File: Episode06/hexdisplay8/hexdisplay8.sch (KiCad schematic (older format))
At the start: 18 parts, among them J1 Conn_02x05_Counter_Clockwise, J2 Conn_02x05_Counter_Clockwise, J3 Conn_01x02, J4 Conn_01x08, J5 Conn_01x06, Q1 MMBT3906, Q2 MMBT3906

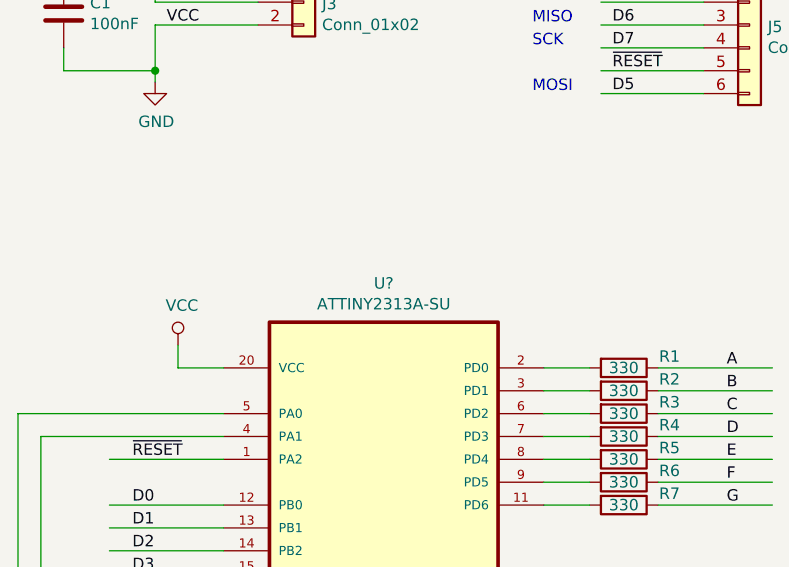
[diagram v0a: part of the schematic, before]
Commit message: assign packages
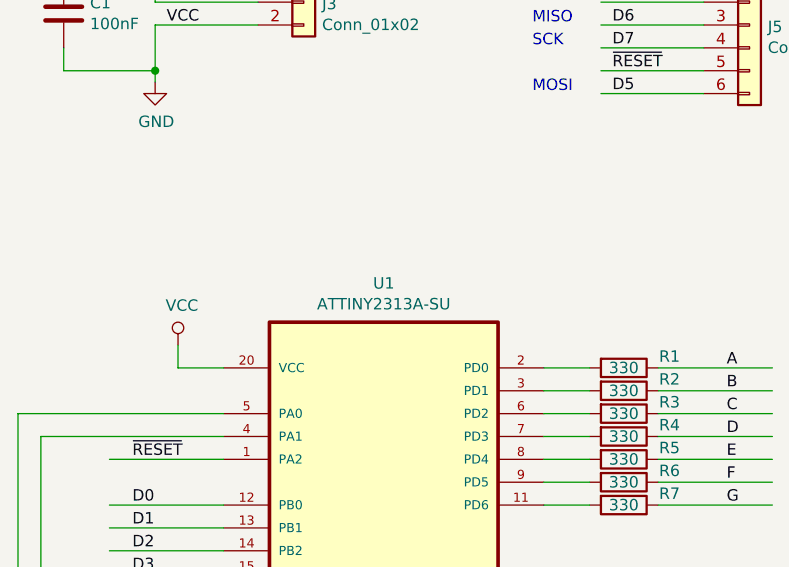
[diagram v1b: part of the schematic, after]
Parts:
- C1: footprint (none) -> Capacitor_SMD:C_1206_3216Metric_Pad1.33x1.80mm_HandSolder
- J1, J2: footprint (none) -> Package_DIP:DIP-10_W7.62mm
- J3: footprint (none) -> Connector_PinHeader_2.54mm:PinHeader_1x02_P2.54mm_Vertical
- J4: footprint (none) -> Connector_PinHeader_2.54mm:PinHeader_1x08_P2.54mm_Vertical
- J5: footprint (none) -> Connector_PinHeader_2.54mm:PinHeader_1x06_P2.54mm_Vertical
- Q1, Q2: footprint SOT95P240X120-3N -> Package_TO_SOT_SMD:SOT-23
- R1, R2, R3, R4, R5, R6, R7, R8, R9: footprint (none) -> Resistor_SMD:R_0805_2012Metric_Pad1.20x1.40mm_HandSolder
- U1: renamed from U?; footprint SOIC127P1032X265-20N -> Package_QFP:LQFP-44_10x10mm_P0.8mm
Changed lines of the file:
@@
 $EndDescr
 $Comp
-L ATTINY2313A-SU:ATTINY2313A-SU U?
+L ATTINY2313A-SU:ATTINY2313A-SU U1
 U 1 1 60451980
 P 2750 3800
-F 0 "U?" H 2750 4770 50  0000 C CNN
+F 0 "U1" H 2750 4770 50  0000 C CNN
 F 1 "ATTINY2313A-SU" H 2750 4679 50  0000 C CNN
-F 2 "SOIC127P1032X265-20N" H 2750 3800 50  0001 L BNN
+F 2 "Package_QFP:LQFP-44_10x10mm_P0.8mm" H 2750 3800 50  0001 L BNN
 F 3 "" H 2750 3800 50  0001 L BNN
 F 4 "Atmel" H 2750 3800 50  0001 L BNN "SUPPLIER"
@@
 F 0 "J2" H 8000 4267 50  0000 C CNN
 F 1 "Conn_02x05_Counter_Clockwise" H 8000 4176 50  0000 C CNN
-F 2 "" H 7950 3850 50  0001 C CNN
+F 2 "Package_DIP:DIP-10_W7.62mm" H 7950 3850 50  0001 C CNN
 F 3 "" H 7950 3850 50  0001 C CNN
 	1    7950 3850
@@
 F 0 "Q1" H 3353 5996 50  0000 L CNN
 F 1 "MMBT3906" H 3353 5905 50  0000 L CNN
-F 2 "SOT95P240X120-3N" H 3200 5950 50  0001 L BNN
+F 2 "Package_TO_SOT_SMD:SOT-23" H 3200 5950 50  0001 L BNN
 F 3 "" H 3200 5950 50  0001 L BNN
 F 4 "Fairchild Semiconductor" H 3200 5950 50  0001 L BNN "MANUFACTURER"
@@
 F 0 "Q2" H 3503 6946 50  0000 L CNN
 F 1 "MMBT3906" H 3503 6855 50  0000 L CNN
-F 2 "SOT95P240X120-3N" H 3350 6900 50  0001 L BNN
+F 2 "Package_TO_SOT_SMD:SOT-23" H 3350 6900 50  0001 L BNN
 F 3 "" H 3350 6900 50  0001 L BNN
 F 4 "Fairchild Semiconductor" H 3350 6900 50  0001 L BNN "MANUFACTURER"
@@
 F 0 "J1" H 8000 3217 50  0000 C CNN
 F 1 "Conn_02x05_Counter_Clockwise" H 8000 3126 50  0000 C CNN
-F 2 "" H 7950 2800 50  0001 C CNN
+F 2 "Package_DIP:DIP-10_W7.62mm" H 7950 2800 50  0001 C CNN
 F 3 "" H 7950 2800 50  0001 C CNN
 	1    7950 2800
@@
 F 0 "J5" H 4430 1692 50  0000 L CNN
 F 1 "Conn_01x06" H 4430 1601 50  0000 L CNN
-F 2 "" H 4350 1700 50  0001 C CNN
+F 2 "Connector_PinHeader_2.54mm:PinHeader_1x06_P2.54mm_Vertical" H 4350 1700 50  0001 C CNN
 F 3 "" H 4350 1700 50  0001 C CNN
 	1    4350 1700
@@
 	1850 3200 1850 3100
 $Comp
-L power:VCC #PWR?
+L power:VCC #PWR0101
 U 1 1 60461FFF
 P 1850 3100
-F 0 "#PWR?" H 1850 2950 50  0001 C CNN
+F 0 "#PWR0101" H 1850 2950 50  0001 C CNN
 F 1 "VCC" H 1867 3273 50  0000 C CNN
 F 2 "" H 1850 3100 50  0001 C CNN
@@
 	1850 4700 1850 4850
 $Comp
-L power:GND #PWR?
+L power:GND #PWR0102
 U 1 1 60462A72
 P 1850 4850
-F 0 "#PWR?" H 1850 4600 50  0001 C CNN
+F 0 "#PWR0102" H 1850 4600 50  0001 C CNN
 F 1 "GND" H 1855 4677 50  0000 C CNN
 F 2 "" H 1850 4850 50  0001 C CNN
@@
 F 0 "R1" V 3750 3400 50  0000 C CNN
 F 1 "330" V 3800 3200 50  0000 C CNN
-F 2 "" V 3730 3200 50  0001 C CNN
+F 2 "Resistor_SMD:R_0805_2012Metric_Pad1.20x1.40mm_HandSolder" V 3730 3200 50  0001 C CNN
 F 3 "" H 3800 3200 50  0001 C CNN
 	1    3800 3200
@@
 F 0 "R2" V 3750 3500 50  0000 C CNN
 F 1 "330" V 3800 3300 50  0000 C CNN
-F 2 "" V 3730 3300 50  0001 C CNN
+F 2 "Resistor_SMD:R_0805_2012Metric_Pad1.20x1.40mm_HandSolder" V 3730 3300 50  0001 C CNN
 F 3 "" H 3800 3300 50  0001 C CNN
 	1    3800 3300
@@
 F 0 "R3" V 3750 3600 50  0000 C CNN
 F 1 "330" V 3800 3400 50  0000 C CNN
-F 2 "" V 3730 3400 50  0001 C CNN
+F 2 "Resistor_SMD:R_0805_2012Metric_Pad1.20x1.40mm_HandSolder" V 3730 3400 50  0001 C CNN
 F 3 "" H 3800 3400 50  0001 C CNN
 	1    3800 3400
@@
 F 0 "R4" V 3750 3700 50  0000 C CNN
 F 1 "330" V 3800 3500 50  0000 C CNN
-F 2 "" V 3730 3500 50  0001 C CNN
+F 2 "Resistor_SMD:R_0805_2012Metric_Pad1.20x1.40mm_HandSolder" V 3730 3500 50  0001 C CNN
 F 3 "" H 3800 3500 50  0001 C CNN
 	1    3800 3500
@@
 F 0 "R5" V 3750 3800 50  0000 C CNN
 F 1 "330" V 3800 3600 50  0000 C CNN
-F 2 "" V 3730 3600 50  0001 C CNN
+F 2 "Resistor_SMD:R_0805_2012Metric_Pad1.20x1.40mm_HandSolder" V 3730 3600 50  0001 C CNN
 F 3 "" H 3800 3600 50  0001 C CNN
 	1    3800 3600
@@
 F 0 "R6" V 3750 3900 50  0000 C CNN
 F 1 "330" V 3800 3700 50  0000 C CNN
-F 2 "" V 3730 3700 50  0001 C CNN
+F 2 "Resistor_SMD:R_0805_2012Metric_Pad1.20x1.40mm_HandSolder" V 3730 3700 50  0001 C CNN
 F 3 "" H 3800 3700 50  0001 C CNN
 	1    3800 3700
@@
 F 0 "R7" V 3750 4000 50  0000 C CNN
 F 1 "330" V 3800 3800 50  0000 C CNN
-F 2 "" V 3730 3800 50  0001 C CNN
+F 2 "Resistor_SMD:R_0805_2012Metric_Pad1.20x1.40mm_HandSolder" V 3730 3800 50  0001 C CNN
 F 3 "" H 3800 3800 50  0001 C CNN
 	1    3800 3800
@@
 F 0 "R8" V 2550 5950 50  0000 C CNN
 F 1 "4k7" V 2650 5950 50  0000 C CNN
-F 2 "" V 2580 5950 50  0001 C CNN
+F 2 "Resistor_SMD:R_0805_2012Metric_Pad1.20x1.40mm_HandSolder" V 2580 5950 50  0001 C CNN
 F 3 "" H 2650 5950 50  0001 C CNN
 	1    2650 5950
@@
 F 0 "R9" V 2700 6900 50  0000 C CNN
 F 1 "4k7" V 2800 6900 50  0000 C CNN
-F 2 "" V 2730 6900 50  0001 C CNN
+F 2 "Resistor_SMD:R_0805_2012Metric_Pad1.20x1.40mm_HandSolder" V 2730 6900 50  0001 C CNN
 F 3 "" H 2800 6900 50  0001 C CNN
 	1    2800 6900
@@
 	4300 5450 4300 5250
 $Comp
-L power:VCC #PWR?
+L power:VCC #PWR0103
 U 1 1 6048B22B
 P 4300 5250
-F 0 "#PWR?" H 4300 5100 50  0001 C CNN
+F 0 "#PWR0103" H 4300 5100 50  0001 C CNN
 F 1 "VCC" H 4317 5423 50  0000 C CNN
 F 2 "" H 4300 5250 50  0001 C CNN
@@
 F 0 "J3" H 2480 1592 50  0000 L CNN
 F 1 "Conn_01x02" H 2480 1501 50  0000 L CNN
-F 2 "" H 2400 1600 50  0001 C CNN
+F 2 "Connector_PinHeader_2.54mm:PinHeader_1x02_P2.54mm_Vertical" H 2400 1600 50  0001 C CNN
 F 3 "" H 2400 1600 50  0001 C CNN
 	1    2400 1600
@@
 	1750 1950 1750 1900
 $Comp
-L power:VCC #PWR?
+L power:VCC #PWR0104
 U 1 1 604BADE0
 P 1750 1350
-F 0 "#PWR?" H 1750 1200 50  0001 C CNN
+F 0 "#PWR0104" H 1750 1200 50  0001 C CNN
 F 1 "VCC" H 1767 1523 50  0000 C CNN
 F 2 "" H 1750 1350 50  0001 C CNN
@@
 $EndComp
 $Comp
-L power:GND #PWR?
+L power:GND #PWR0105
 U 1 1 604BB1BF
 P 1750 1950
-F 0 "#PWR?" H 1750 1700 50  0001 C CNN
+F 0 "#PWR0105" H 1750 1700 50  0001 C CNN
 F 1 "GND" H 1755 1777 50  0000 C CNN
 F 2 "" H 1750 1950 50  0001 C CNN
@@
 F 0 "C1" H 1465 1696 50  0000 L CNN
 F 1 "100nF" H 1465 1605 50  0000 L CNN
-F 2 "" H 1388 1500 50  0001 C CNN
+F 2 "Capacitor_SMD:C_1206_3216Metric_Pad1.33x1.80mm_HandSolder" H 1388 1500 50  0001 C CNN
 F 3 "" H 1350 1650 50  0001 C CNN
 	1    1350 1650
@@
 F 0 "J4" H 6130 5142 50  0000 L CNN
 F 1 "Conn_01x08" H 6130 5051 50  0000 L CNN
-F 2 "" H 6050 5150 50  0001 C CNN
+F 2 "Connector_PinHeader_2.54mm:PinHeader_1x08_P2.54mm_Vertical" H 6050 5150 50  0001 C CNN
 F 3 "" H 6050 5150 50  0001 C CNN
 	1    6050 5150

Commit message: use correct package for attiny2313a
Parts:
- U1: footprint Package_QFP:LQFP-44_10x10mm_P0.8mm -> Package_SO:SOIC-20W_7.5x12.8mm_P1.27mm
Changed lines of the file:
@@
 F 0 "U1" H 2750 4770 50  0000 C CNN
 F 1 "ATTINY2313A-SU" H 2750 4679 50  0000 C CNN
-F 2 "Package_QFP:LQFP-44_10x10mm_P0.8mm" H 2750 3800 50  0001 L BNN
+F 2 "Package_SO:SOIC-20W_7.5x12.8mm_P1.27mm" H 2750 3800 50  0001 L BNN
 F 3 "" H 2750 3800 50  0001 L BNN
 F 4 "Atmel" H 2750 3800 50  0001 L BNN "SUPPLIER"
